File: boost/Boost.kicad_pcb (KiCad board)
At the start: 2 copper layers, 19 parts, among them P1 CONN_01X02, P2 CONN_01X02, U1 TPS61087

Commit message: Initial Layout
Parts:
- D1: value D_Schottky -> B340LA-13-F
- L1: value INDUCTOR -> SRU1048
- R1: value 100K -> 57K6
- R2: value R -> 150K
- R3: value R -> 39K
- moved C4 99.2 mm to (113.9, 66.9), turned to 90 degrees
- moved C5 94.8 mm to (110.3, 66.7), turned to 90 degrees
- moved C3 93.5 mm to (120.5, 68.7), turned to 180 degrees
- moved R1 93.4 mm to (113.7, 70.9), turned to 180 degrees
- moved R3 91.8 mm to (113.4, 82.3), turned to 270 degrees
- moved R2 88.5 mm to (115.4, 77.3), turned to 180 degrees
- moved C2 87.5 mm to (119.9, 64.6), turned to 180 degrees
- moved C1 79.5 mm to (119.9, 61.6), turned to 180 degrees
- moved C6 77.1 mm to (120.6, 88.4), turned to 180 degrees
- moved P1 76.6 mm to (121.5, 57.6), turned to 270 degrees
- moved C8 74.0 mm to (120.5, 95.3), turned to 180 degrees
- moved C7 69.4 mm to (120.5, 91.9), turned to 180 degrees
- moved TP1 65.5 mm to (139.8, 59.0)
- moved C9 61.6 mm to (120.5, 98.9), turned to 180 degrees
- moved D1 59.7 mm to (128.3, 83.8), turned to 90 degrees
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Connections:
- net Net-(C1-Pad1) renamed /Vin
- net Net-(C6-Pad1) renamed /Vout
- net Net-(D1-Pad2) renamed /SW
- U1 pad 11: (no net) -> GND
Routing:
- net Net-(C4-Pad1): track 0.00 -> 12.6 mm, vias 0 -> 2
- net Net-(R2-Pad2): track 0.00 -> 11.5 mm
- net /Vin: track 0.00 -> 11.3 mm, vias 0 -> 2
- net Net-(C5-Pad1): track 0.00 -> 4.85 mm
- net Net-(R1-Pad1): track 0.00 -> 3.37 mm
- added copper zone on F.Cu, net /SW
- added copper zone on F.Cu, net /Vin
- added copper zone on F.Cu, net /Vout
- added copper zone on F.Cu, net GND
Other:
- board text added: "GND"
- board text added: "VIN"
- board text added: "VOUT"

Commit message: Finished layout
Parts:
- added REF**111111: STITCH-VIA, Boost:STITCH-VIA, F.Cu at (109.7, 57.4)
- added REF**1111111: STITCH-VIA, Boost:STITCH-VIA, F.Cu at (109.7, 86.4)
- added REF**1111112: STITCH-VIA, Boost:STITCH-VIA, F.Cu at (109.7, 88.9)
- added REF**1111113: STITCH-VIA, Boost:STITCH-VIA, F.Cu at (109.7, 91.4)
- added REF**1111114: STITCH-VIA, Boost:STITCH-VIA, F.Cu at (109.7, 94.0)
- added REF**1111115: STITCH-VIA, Boost:STITCH-VIA, F.Cu at (109.7, 96.5)
- added REF**1111116: STITCH-VIA, Boost:STITCH-VIA, F.Cu at (109.7, 99.1)
- added REF**1111117: STITCH-VIA, Boost:STITCH-VIA, F.Cu at (109.7, 101.6)
- added REF**1111118: STITCH-VIA, Boost:STITCH-VIA, F.Cu at (109.7, 104.1)
- added REF**111112: STITCH-VIA, Boost:STITCH-VIA, F.Cu at (109.7, 59.4)
- added REF**1111121: STITCH-VIA, Boost:STITCH-VIA, F.Cu at (112.3, 86.4)
- added REF**1111122: STITCH-VIA, Boost:STITCH-VIA, F.Cu at (112.3, 88.9)
- added REF**1111123: STITCH-VIA, Boost:STITCH-VIA, F.Cu at (112.3, 91.4)
- added REF**1111124: STITCH-VIA, Boost:STITCH-VIA, F.Cu at (112.3, 94.0)
- added REF**1111125: STITCH-VIA, Boost:STITCH-VIA, F.Cu at (112.3, 96.5)
- added REF**1111126: STITCH-VIA, Boost:STITCH-VIA, F.Cu at (112.3, 99.1)
- added REF**1111127: STITCH-VIA, Boost:STITCH-VIA, F.Cu at (112.3, 101.6)
- added REF**1111128: STITCH-VIA, Boost:STITCH-VIA, F.Cu at (112.3, 104.1)
- added REF**111113: STITCH-VIA, Boost:STITCH-VIA, F.Cu at (109.7, 61.5)
- added REF**1111131: STITCH-VIA, Boost:STITCH-VIA, F.Cu at (114.8, 86.4)
- added REF**1111132: STITCH-VIA, Boost:STITCH-VIA, F.Cu at (114.8, 88.9)
- added REF**1111133: STITCH-VIA, Boost:STITCH-VIA, F.Cu at (114.8, 91.4)
- added REF**1111134: STITCH-VIA, Boost:STITCH-VIA, F.Cu at (114.8, 94.0)
- added REF**1111135: STITCH-VIA, Boost:STITCH-VIA, F.Cu at (114.8, 96.5)
- added REF**1111136: STITCH-VIA, Boost:STITCH-VIA, F.Cu at (114.8, 99.1)
- added REF**1111137: STITCH-VIA, Boost:STITCH-VIA, F.Cu at (114.8, 101.6)
- added REF**1111138: STITCH-VIA, Boost:STITCH-VIA, F.Cu at (114.8, 104.1)
- added REF**111121: STITCH-VIA, Boost:STITCH-VIA, F.Cu at (111.8, 57.4)
- added REF**111122: STITCH-VIA, Boost:STITCH-VIA, F.Cu at (111.8, 59.4)
- added REF**111123: STITCH-VIA, Boost:STITCH-VIA, F.Cu at (111.8, 61.5)
- added REF**111131: STITCH-VIA, Boost:STITCH-VIA, F.Cu at (113.8, 57.4)
- added REF**111132: STITCH-VIA, Boost:STITCH-VIA, F.Cu at (113.8, 59.4)
- added REF**111133: STITCH-VIA, Boost:STITCH-VIA, F.Cu at (113.8, 61.5)
- moved TP1 10.7 mm to (129.0, 59.4)
- moved L1 9.02 mm to (128.5, 71.7)
- moved TP2 7.99 mm to (128.5, 94.0)
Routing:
- net /Vout: track 0.00 -> 14.6 mm, vias 0 -> 2
- added copper zone on B.Cu, net GND
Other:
- board outline added: 25.4 x 49.8 mm
- board text added: "Power Swap Boost"
- board text added: "Rev 1"

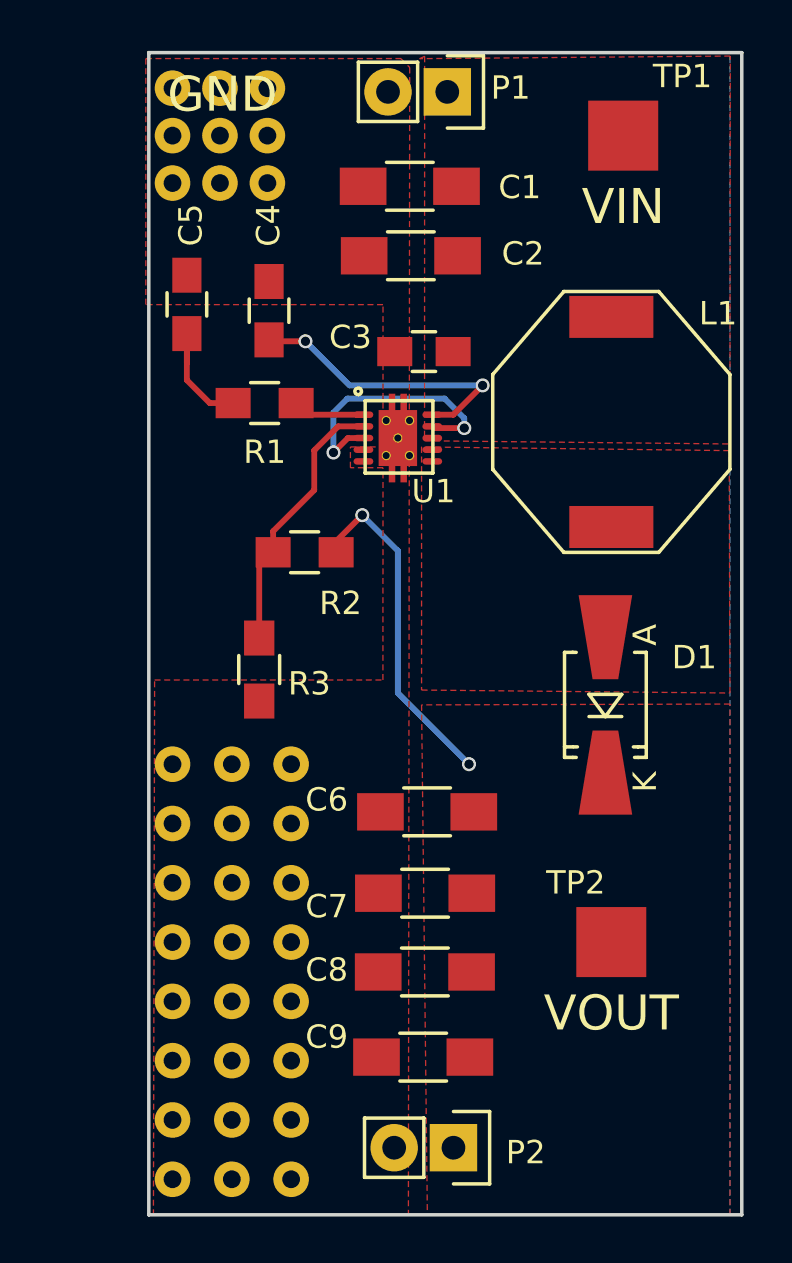
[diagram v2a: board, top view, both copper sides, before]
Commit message: Added indicator LED, mounting holes and a logo.
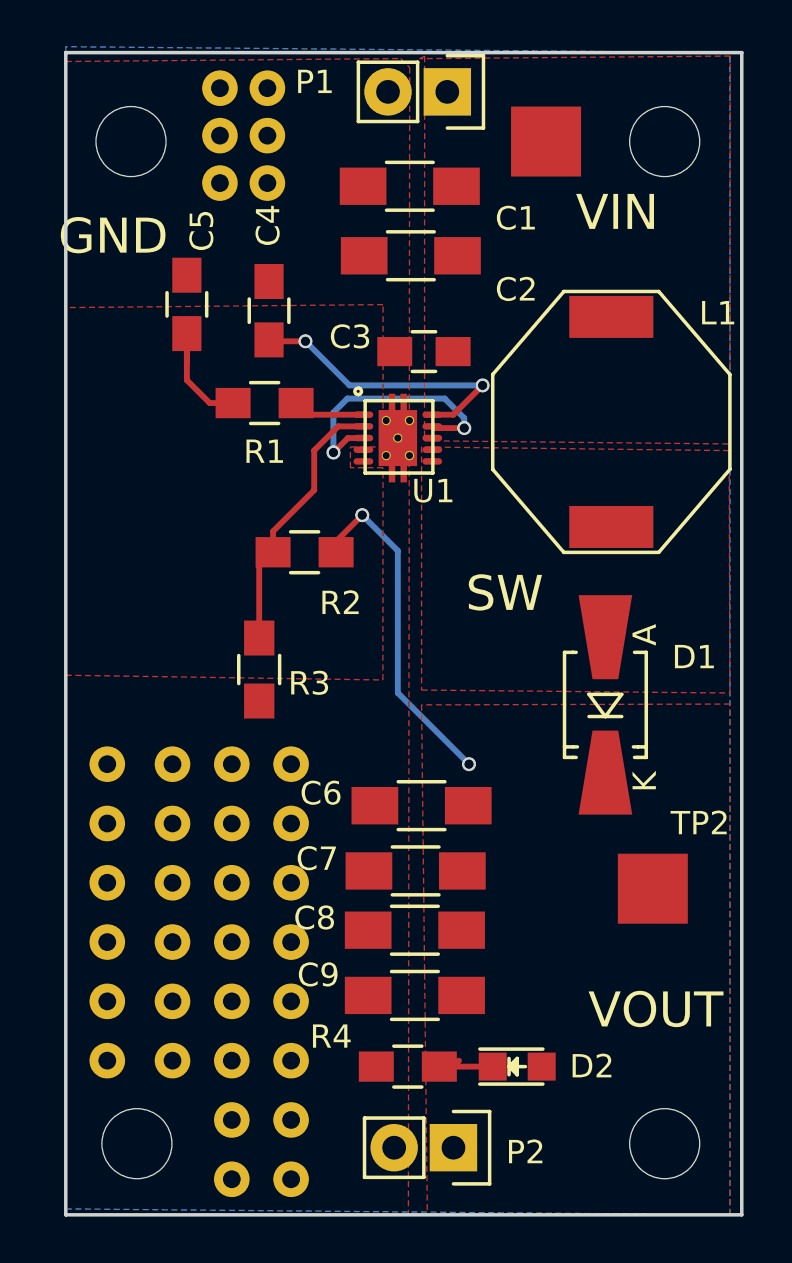
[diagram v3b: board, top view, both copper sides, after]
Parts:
- removed REF**111111, REF**1111117, REF**1111118, REF**111112, REF**111113: STITCH-VIA, Boost:STITCH-VIA
- added D2: LED, LEDs:LED-0805, F.Cu at (124.5, 99.3)
- added G***: LOGO, Boost:PS, B.Cu at (120.2, 62.9)
- added R4: 500, Resistors_SMD:R_0805_HandSoldering, F.Cu at (119.8, 99.3)
- added REF**: MountingHole_3mm, Mounting_Holes:MountingHole_3mm, F.Cu at (108.2, 102.6)
- added REF**: MountingHole_3mm, Mounting_Holes:MountingHole_3mm, F.Cu at (108.0, 59.7)
- added REF**: MountingHole_3mm, Mounting_Holes:MountingHole_3mm, F.Cu at (130.8, 59.7)
- added REF**: MountingHole_3mm, Mounting_Holes:MountingHole_3mm, F.Cu at (130.8, 102.6)
- added REF**1111111: STITCH-VIA, Boost:STITCH-VIA, F.Cu at (106.9, 86.4)
- added REF**1111112: STITCH-VIA, Boost:STITCH-VIA, F.Cu at (106.9, 88.9)
- added REF**1111113: STITCH-VIA, Boost:STITCH-VIA, F.Cu at (106.9, 91.4)
- added REF**1111114: STITCH-VIA, Boost:STITCH-VIA, F.Cu at (106.9, 94.0)
- added REF**1111115: STITCH-VIA, Boost:STITCH-VIA, F.Cu at (106.9, 96.5)
- added REF**1111116: STITCH-VIA, Boost:STITCH-VIA, F.Cu at (106.9, 99.1)
- moved TP1 3.31 mm to (125.7, 59.7)
- moved TP2 2.90 mm to (130.3, 91.7)
- moved C9 2.67 mm to (120.1, 96.3)
- moved C8 1.84 mm to (120.1, 93.5)
- moved C7 1.04 mm to (120.1, 90.9)
- moved C6 0.36 mm to (120.4, 88.1)
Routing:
- net Net-(D2-Pad1): track 0.00 -> 2.65 mm
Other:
- board size 25.4 x 49.8 mm -> 29 x 49.8 mm
- board text added: "SW"

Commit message: Gerber generation for Rev 1 proto
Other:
- rule trace_min: 0.2 -> 0.1524
- rule via_min_size: 0.4 -> 0.3302
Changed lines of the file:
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@@
 (kicad_pcb (version 4) (host pcbnew 0.201509151501+6198~30~ubuntu14.04.1-product)
   (general
-    (links 0)
-    (no_connects 2)
-    (area 105.080999 55.804999 134.187001 105.739001)
+    (links 83)
+    (no_connects 0)
+    (area 101.182809 52.453146 139.300046 108.59226)
     (thickness 1.6)
     (drawings 10)
@@
     (zone_clearance 0.254)
     (zone_45_only no)
-    (trace_min 0.2)
+    (trace_min 0.1524)
     (segment_width 0.2)
     (edge_width 0.15)
     (via_size 0.6)
     (via_drill 0.4)
-    (via_min_size 0.4)
+    (via_min_size 0.3302)
     (via_min_drill 0.3)
     (uvia_size 0.3)
@@
     (visible_elements FFFEFF7F)
     (pcbplotparams
-      (layerselection 0x00030_80000001)
+      (layerselection 0x010fc_80000001)
       (usegerberextensions false)
       (excludeedgelayer true)
@@
       (plotinvisibletext false)
       (padsonsilk false)
-      (subtractmaskfromsilk false)
+      (subtractmaskfromsilk true)
       (outputformat 1)
       (mirror false)
-      (drillshape 1)
+      (drillshape 0)
       (scaleselection 1)
       (outputdirectory ""))
